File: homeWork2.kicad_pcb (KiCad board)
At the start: 2 copper layers, 115 x 97.8 mm, 48 parts, among them J1 Barrel_Jack_Switch_SMT, J2 0.100_2Pin, J3 0.100_2Pin, U1 LM7805_TO220

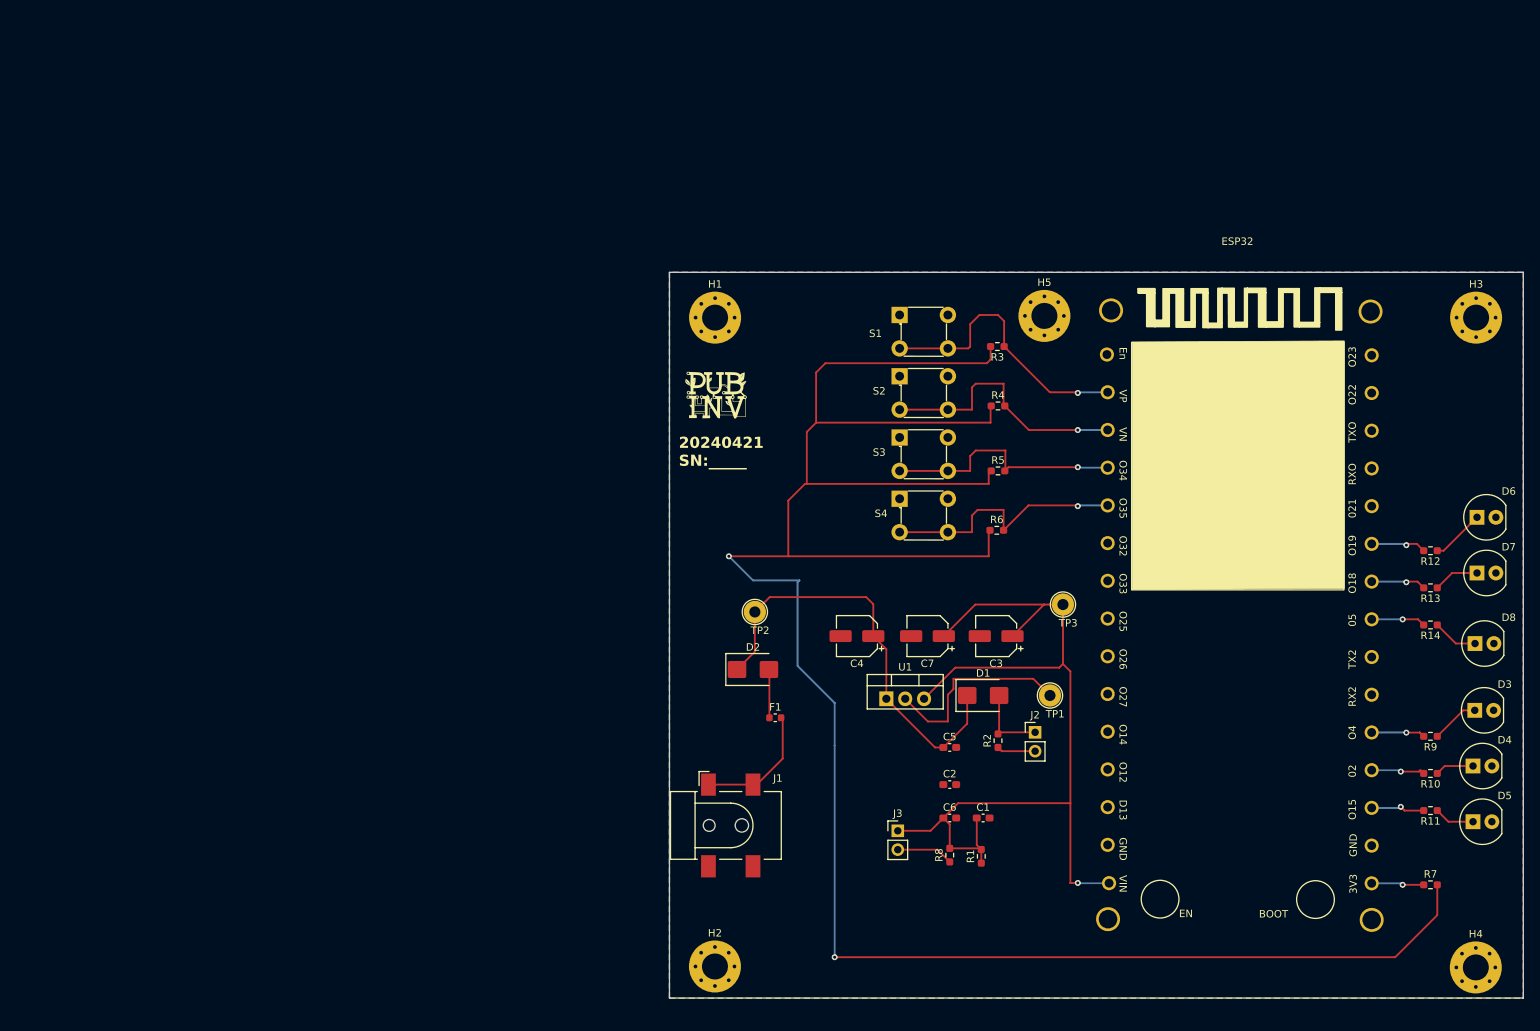
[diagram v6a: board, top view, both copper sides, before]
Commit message: the coordinates of the PCB changed, the upper corner is set to x=50 y=50. The edgecut measurement is adjusted to integer metric dimension. The mounting holes are also put on well adjusted integer metric dimention and locked. The same is done for the barrel jack and additionally it is moved outside the edgecut exactly 3.00 mm. User Drawing dimensions are also added.
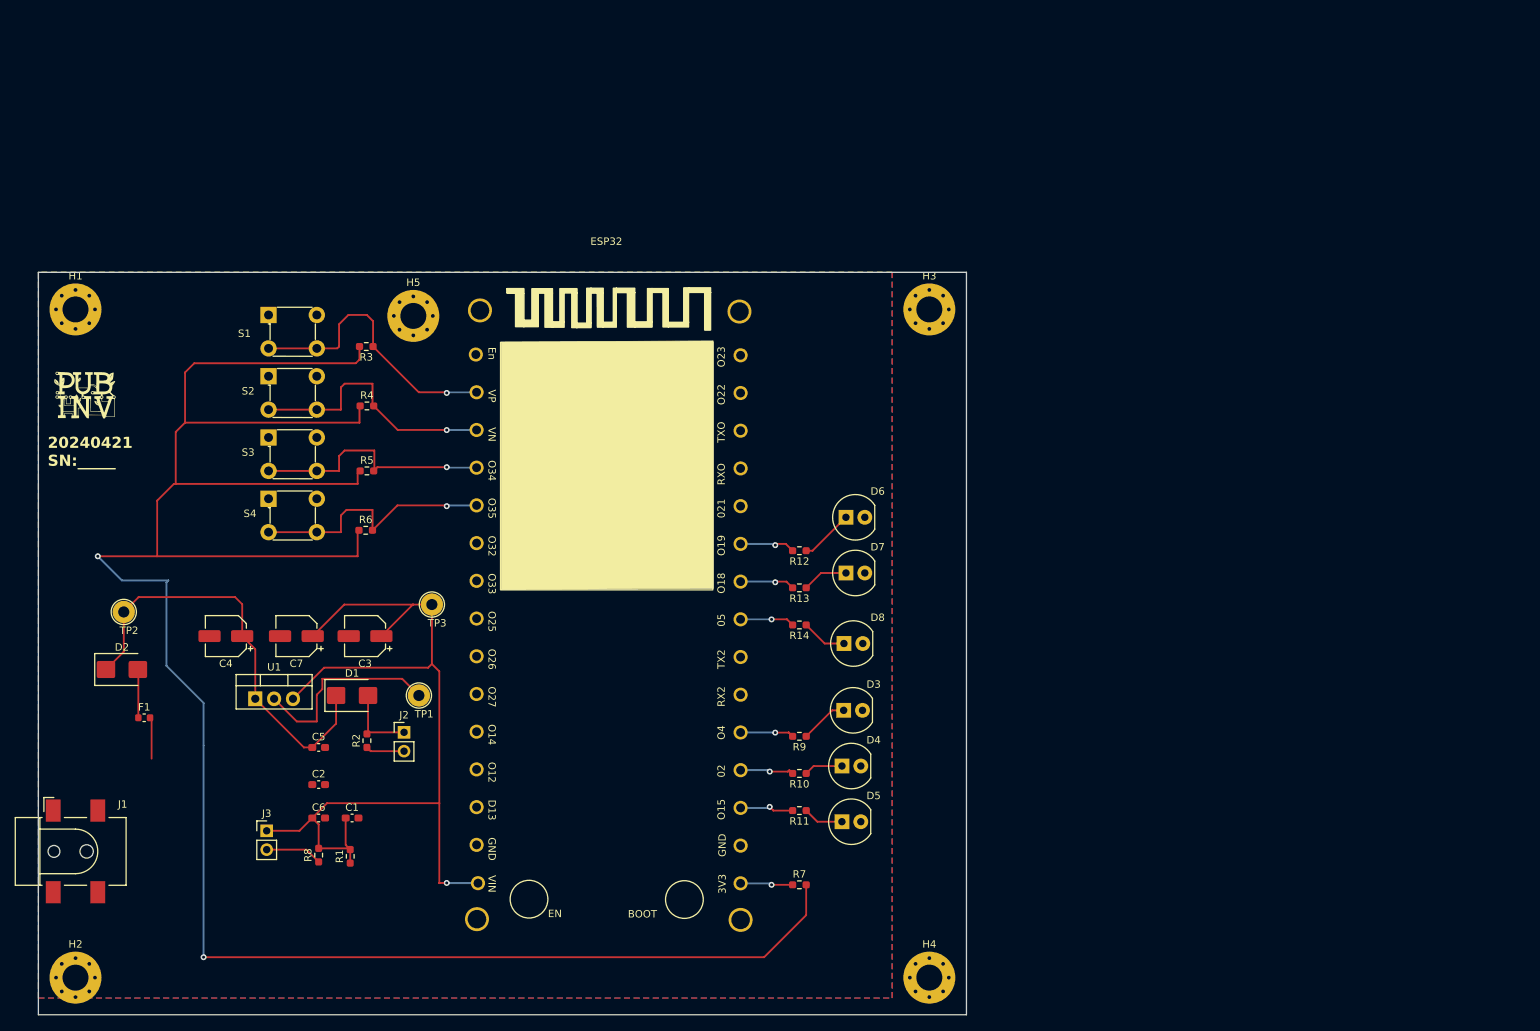
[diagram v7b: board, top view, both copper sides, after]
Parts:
- moved J1 88.3 mm to (55.0, 128.0)
- moved H1 86.2 mm to (55.0, 55.0)
- moved H2 86.1 mm to (55.0, 145.0)
- moved U1 85.0 mm to (79.2, 107.4)
- moved C1 85.0 mm to (92.2, 123.5)
- moved C2 85.0 mm to (87.8, 119.0)
- moved C3 85.0 mm to (94.0, 99.0)
- moved C4 85.0 mm to (75.2, 99.0)
- moved C5 85.0 mm to (87.8, 114.0)
- moved C6 85.0 mm to (87.8, 123.5)
- moved C7 85.0 mm to (84.8, 99.0)
- moved D1 85.0 mm to (92.2, 107.0)
- moved D2 85.0 mm to (61.2, 103.5)
- moved D3 85.0 mm to (161.0, 109.0)
- moved D4 85.0 mm to (160.8, 116.5)
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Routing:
- net Net-(F1-Pad2): track 17.0 -> 5.84 mm
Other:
- board size 115 x 97.8 mm -> 125 x 100 mm

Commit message: Four Net Classes are added, default, ground, and two classes for power, one for 5 volts and another for 3.3 volts.The width of the traces used allows 40 degrees Celius temperature rise of the component.
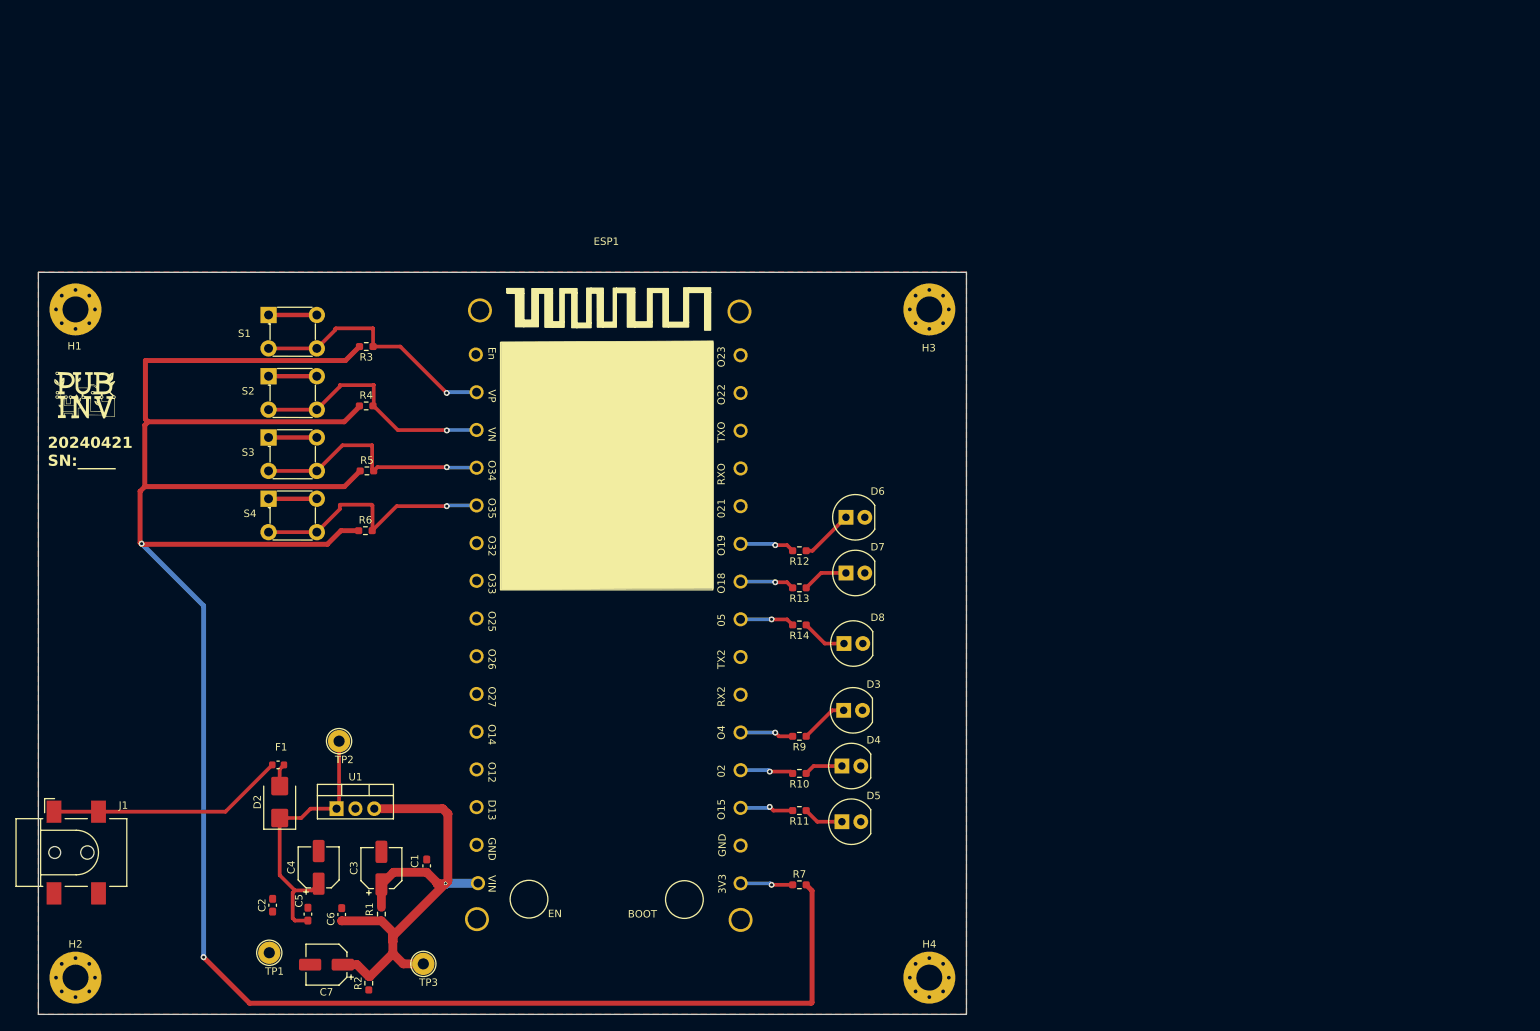
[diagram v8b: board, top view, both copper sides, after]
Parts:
- removed D1: D_Schottky, Diode_SMD:D_SMB
- removed H5: MountingHole_Pad_3.5mm, PubInv_KiCad_PCB:MountingHole_3.5mm_Pad_Via
- removed J2, J3: 0.100_2Pin, Connector_PinHeader_2.54mm:PinHeader_1x02_P2.54mm_Vertical
- removed R8: R, Resistor_SMD:R_0603_1608Metric_Pad0.98x0.95mm_HandSolder
- C1, C5, C6: value C -> 100nF
- C2: value C -> 39pF
- C3, C4, C7: value C_Polarized -> 47uF 16V
- R10, R11, R12, R13, R14, R9: value R -> 60 ohm
- R2: value R -> 330R
- R3, R4, R5, R6: value R -> 10 k
- R7: value R -> 1 Ohm
- moved TP3 48.4 mm to (101.8, 143.2)
- moved C7 44.4 mm to (88.8, 143.2)
- moved TP1 40.1 mm to (81.1, 141.7)
- moved TP2 33.8 mm to (90.5, 113.2)
- moved C4 33.6 mm to (87.8, 130.2), turned to 90 degrees
- moved R2 32.7 mm to (94.5, 145.8)
- moved C3 31.3 mm to (96.2, 130.2), turned to 90 degrees
- moved D2 27.8 mm to (82.5, 121.3), turned to 90 degrees
- moved C5 22.5 mm to (86.3, 136.4), turned to 90 degrees
- moved F1 19.1 mm to (82.3, 116.3), turned to 180 degrees
- moved U1 18.4 mm to (90.2, 122.2)
- moved C2 17.4 mm to (81.5, 135.2), turned to 90 degrees
- moved C6 13.4 mm to (90.8, 136.5), turned to 90 degrees
- moved C1 11.9 mm to (102.3, 129.9), turned to 90 degrees
- moved R1 8.84 mm to (96.2, 136.4)
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- renumbered ESP32 to ESP1
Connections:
- ESP1 pad 2: unconnected-(ESP1-GND-Pad2) -> GND
- R2 pad 1: ControllerVcc -> Net-(D1-Pad1)
- R2 pad 2: Net-(D1-A) -> +5V
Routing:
- net +5V: track 127.8 -> 72.7 mm
- net Net-(F1-Pad2): track 5.84 -> 32.0 mm
- net Vin: track 58.1 -> 37.6 mm
- net Net-(D1-A): track 10.3 -> 0.00 mm
- net +3.3V: track 294.3 -> 304.1 mm
- net VBus: track 7.68 -> 0.00 mm
- net ControllerVcc: track 5.21 -> 0.00 mm
- net Net-(ESP1-VP): track 38.0 -> 34.3 mm
- net Net-(D2-A): track 6.53 -> 3.09 mm
- net Net-(ESP1-VN): track 35.5 -> 33.7 mm
- net GND: track 27.0 -> 26.1 mm
- removed copper zone on B.Cu, net GND
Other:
- board size 125 x 100 mm -> 125 x 99.9 mm
